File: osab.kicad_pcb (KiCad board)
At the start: 2 copper layers, 60 x 100 mm, 152 parts, among them CON1 TF-01A, CON2 PJ-3420-A-SMT, CON3 TYPE-C-31-M-12, Q1 BC847B, SW1 PPP, SW10 RESET, SW2 VOL-, SW3 VOL+, SW4 CHAP-, SW5 CHAP+, SW6 OT/NT, SW7 BOOK-, SW8 BOOK+, SW9 BUTTON_LOCK, U1 VS1000, U2 ME6211C33M5G-N, U3 25LC640A, U4 TP4055, U5 MF5853CS, U6 TCS7191, Y1 12MHz

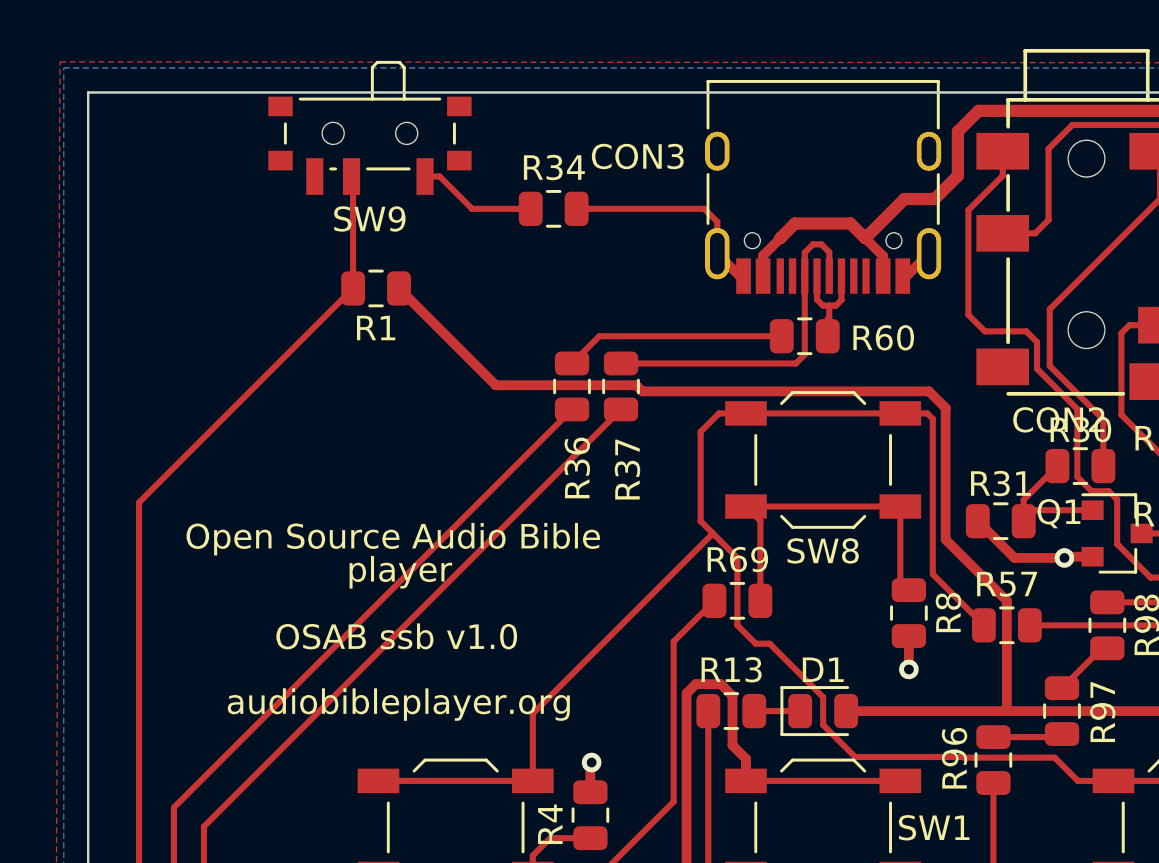
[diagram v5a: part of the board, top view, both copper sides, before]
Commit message: single-sided: Moved button lock back 5.75 mm
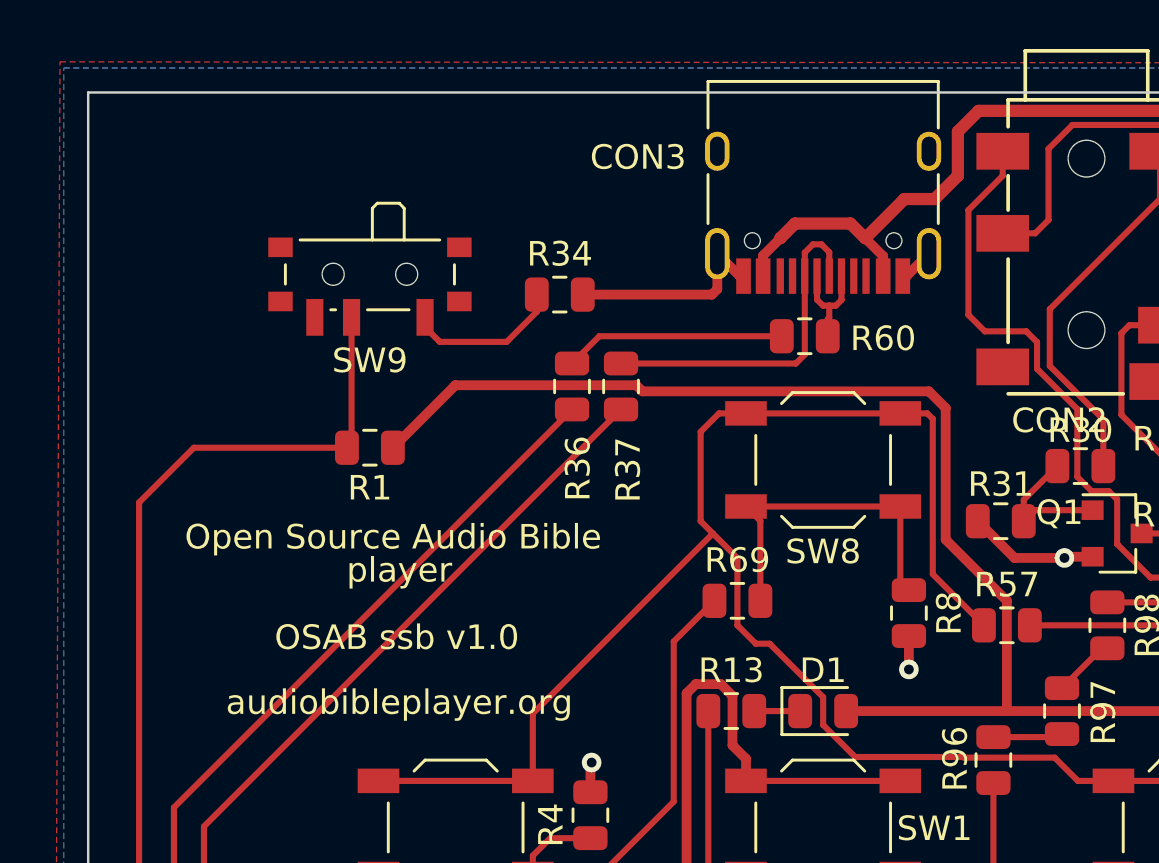
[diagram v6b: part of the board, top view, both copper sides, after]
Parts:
- moved R1 6.50 mm to (126.5, 61.5)
- moved SW9 5.75 mm to (126.5, 54.8)
- moved R34 3.51 mm to (134.2, 55.2)
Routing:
- net Net-(R1-Pad2): track 57.9 -> 55.8 mm
- net Net-(R34-Pad1): track 4.86 -> 6.42 mm
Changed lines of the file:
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@@
     (thickness 1.6)
     (drawings 12)
-    (tracks 1110)
+    (tracks 1111)
     (zones 0)
     (modules 152)
@@
   )
   (module Button_Switch_SMD:SW_SPDT_PCM12 (layer F.Cu)
-    (at 126.5 49 180)
+    (at 126.5 54.75 180)
     (descr "Ultraminiature Surface Mount Slide Switch, right-angle, https://www.ckswitches.com/media/1424/pcm.pdf")
     (attr smd)
@@
   )
   (module Resistor_SMD:R_0805_2012Metric (layer F.Cu)
-    (at 126.75 55 180)
+    (at 126.5 61.5 180)
     (descr "Resistor SMD 0805 (2012 Metric), square (rectangular) end terminal, IPC_7351 nominal, (Body size source: https://docs.google.com/spreadsheets/d/1BsfQQcO9C6DZCsRaXUlFlo91Tg2WpOkGARC1WS5S8t0/edit?usp=sharing), generated with kicad-footprint-generator")
     (tags resistor)
@@
   )
   (module Resistor_SMD:R_0805_2012Metric (layer F.Cu)
-    (at 134 51.75)
+    (at 134.25 55.25)
     (descr "Resistor SMD 0805 (2012 Metric), square (rectangular) end terminal, IPC_7351 nominal, (Body size source: https://docs.google.com/spreadsheets/d/1BsfQQcO9C6DZCsRaXUlFlo91Tg2WpOkGARC1WS5S8t0/edit?usp=sharing), generated with kicad-footprint-generator")
     (tags resistor)
@@
   (segment (start 148.405 54.495) (end 149.32 53.58) (width 0.4) (layer F.Cu) (net 2) (status 30))
   (segment (start 148.25 54.495) (end 148.405 54.495) (width 0.4) (layer F.Cu) (net 2) (status 30))
-  (segment (start 140.68 52.28) (end 140.68 53.58) (width 0.25) (layer F.Cu) (net 2))
-  (segment (start 140.15 51.75) (end 140.68 52.28) (width 0.25) (layer F.Cu) (net 2))
-  (segment (start 134.9375 51.75) (end 140.15 51.75) (width 0.25) (layer F.Cu) (net 2))
+  (segment (start 140.68 55.03) (end 140.68 53.58) (width 0.4) (layer F.Cu) (net 2))
+  (segment (start 140.46 55.25) (end 140.68 55.03) (width 0.4) (layer F.Cu) (net 2))
+  (segment (start 135.1875 55.25) (end 140.46 55.25) (width 0.4) (layer F.Cu) (net 2))
   (segment (start 146.1 127.0875) (end 146.9375 126.25) (width 0.25) (layer F.Cu) (net 3) (status 20))
   (segment (start 146.1 128.15) (end 146.1 127.0875) (width 0.25) (layer F.Cu) (net 3) (status 10))
@@
   (segment (start 140.29999 121.372926) (end 140.29999 119.95001) (width 0.4) (layer F.Cu) (net 8))
   (segment (start 139.822906 121.85001) (end 140.29999 121.372926) (width 0.4) (layer F.Cu) (net 8))
-  (segment (start 150 59.879998) (end 150 65.25) (width 0.4) (layer F.Cu) (net 8))
-  (segment (start 150 65.25) (end 152.5 67.75) (width 0.4) (layer F.Cu) (net 8))
-  (segment (start 149.320001 59.199999) (end 150 59.879998) (width 0.4) (layer F.Cu) (net 8))
-  (segment (start 137.622915 59.199999) (end 149.320001 59.199999) (width 0.4) (layer F.Cu) (net 8))
   (segment (start 145.9375 72.25) (end 152.5 72.25) (width 0.4) (layer F.Cu) (net 8) (status 10))
-  (segment (start 131.63751 58.95001) (end 137.372926 58.95001) (width 0.4) (layer F.Cu) (net 8))
-  (segment (start 152.5 67.75) (end 152.5 72.25) (width 0.4) (layer F.Cu) (net 8))
-  (segment (start 127.6875 55) (end 131.63751 58.95001) (width 0.4) (layer F.Cu) (net 8) (status 10))
-  (segment (start 137.372926 58.95001) (end 137.622915 59.199999) (width 0.4) (layer F.Cu) (net 8))
   (segment (start 162.5 72.25) (end 152.5 72.25) (width 0.4) (layer F.Cu) (net 8))
   (segment (start 169.5 79.25) (end 162.5 72.25) (width 0.4) (layer F.Cu) (net 8))
@@
   (segment (start 150 120.25) (end 150.149999 120.399999) (width 0.5) (layer F.Cu) (net 8))
   (segment (start 147.45 117.75) (end 147.95 117.75) (width 0.25) (layer F.Cu) (net 8))
+  (segment (start 129.98749 58.95001) (end 127.4375 61.5) (width 0.4) (layer F.Cu) (net 8))
+  (segment (start 137.372926 58.95001) (end 129.98749 58.95001) (width 0.4) (layer F.Cu) (net 8))
+  (segment (start 137.622915 59.199999) (end 137.372926 58.95001) (width 0.4) (layer F.Cu) (net 8))
+  (segment (start 152.5 67.75) (end 150 65.25) (width 0.4) (layer F.Cu) (net 8))
+  (segment (start 152.5 72.25) (end 152.5 67.75) (width 0.4) (layer F.Cu) (net 8))
+  (segment (start 150 65.25) (end 150 59.879998) (width 0.4) (layer F.Cu) (net 8))
+  (segment (start 150 59.879998) (end 149.320001 59.199999) (width 0.4) (layer F.Cu) (net 8))
+  (segment (start 149.320001 59.199999) (end 137.622915 59.199999) (width 0.4) (layer F.Cu) (net 8))
   (segment (start 158.1625 116.25) (end 154.6625 116.25) (width 0.25) (layer F.Cu) (net 9) (status 30))
   (segment (start 157.975 130.6875) (end 160.1 130.6875) (width 0.4) (layer F.Cu) (net 10) (status 30))
@@
   (segment (start 165.7125 65.6) (end 166.3125 65) (width 0.25) (layer F.Cu) (net 28) (status 20))
   (segment (start 161.43315 65.6) (end 165.7125 65.6) (width 0.25) (layer F.Cu) (net 28))
-  (segment (start 125.8125 50.4925) (end 125.75 50.43) (width 0.25) (layer F.Cu) (net 29) (status 30))
-  (segment (start 125.8125 55) (end 125.8125 50.4925) (width 0.25) (layer F.Cu) (net 29) (status 30))
-  (segment (start 125.326973 55.485527) (end 125.8125 55) (width 0.25) (layer F.Cu) (net 29) (status 20))
-  (segment (start 117.076973 63.735527) (end 125.326973 55.485527) (width 0.25) (layer F.Cu) (net 29))
   (segment (start 117.076973 104.014473) (end 117.076973 63.735527) (width 0.25) (layer F.Cu) (net 29))
   (segment (start 117.5625 104.5) (end 117.076973 104.014473) (width 0.25) (layer F.Cu) (net 29) (status 10))
+  (segment (start 119.3125 61.5) (end 125.5625 61.5) (width 0.25) (layer F.Cu) (net 29))
+  (segment (start 117.076973 63.735527) (end 119.3125 61.5) (width 0.25) (layer F.Cu) (net 29))
+  (segment (start 125.75 61.3125) (end 125.5625 61.5) (width 0.25) (layer F.Cu) (net 29))
+  (segment (start 125.75 56.18) (end 125.75 61.3125) (width 0.25) (layer F.Cu) (net 29))
   (segment (start 122.95 98.9) (end 128.15 98.9) (width 0.25) (layer F.Cu) (net 30) (status 20))
   (segment (start 121.85 98.9) (end 122.95 98.9) (width 0.25) (layer F.Cu) (net 30) (status 10))
@@
   (segment (start 136.5 140.3125) (end 136.4375 140.25) (width 0.25) (layer F.Cu) (net 45) (status 30))
   (segment (start 136.5 143.5625) (end 136.5 140.3125) (width 0.25) (layer F.Cu) (net 45) (status 30))
-  (segment (start 130.67 51.75) (end 132.575 51.75) (width 0.25) (layer F.Cu) (net 46) (status 20))
-  (segment (start 129.35 50.43) (end 130.67 51.75) (width 0.25) (layer F.Cu) (net 46))
-  (segment (start 132.575 51.75) (end 133.0625 51.75) (width 0.25) (layer F.Cu) (net 46) (status 30))
-  (segment (start 128.75 50.43) (end 129.35 50.43) (width 0.25) (layer F.Cu) (net 46) (status 10))
+  (segment (start 128.75 56.58) (end 128.75 56.18) (width 0.25) (layer F.Cu) (net 46))
+  (segment (start 132.0825 57.18) (end 129.35 57.18) (width 0.25) (layer F.Cu) (net 46))
+  (segment (start 133.3125 55.95) (end 132.0825 57.18) (width 0.25) (layer F.Cu) (net 46))
+  (segment (start 129.35 57.18) (end 128.75 56.58) (width 0.25) (layer F.Cu) (net 46))
+  (segment (start 133.3125 55.25) (end 133.3125 55.95) (width 0.25) (layer F.Cu) (net 46))
   (segment (start 119.199978 101.184932) (end 119.199978 92.815068) (width 0.25) (layer F.Cu) (net 47))
   (segment (start 121.815068 103.800022) (end 119.199978 101.184932) (width 0.25) (layer F.Cu) (net 47))

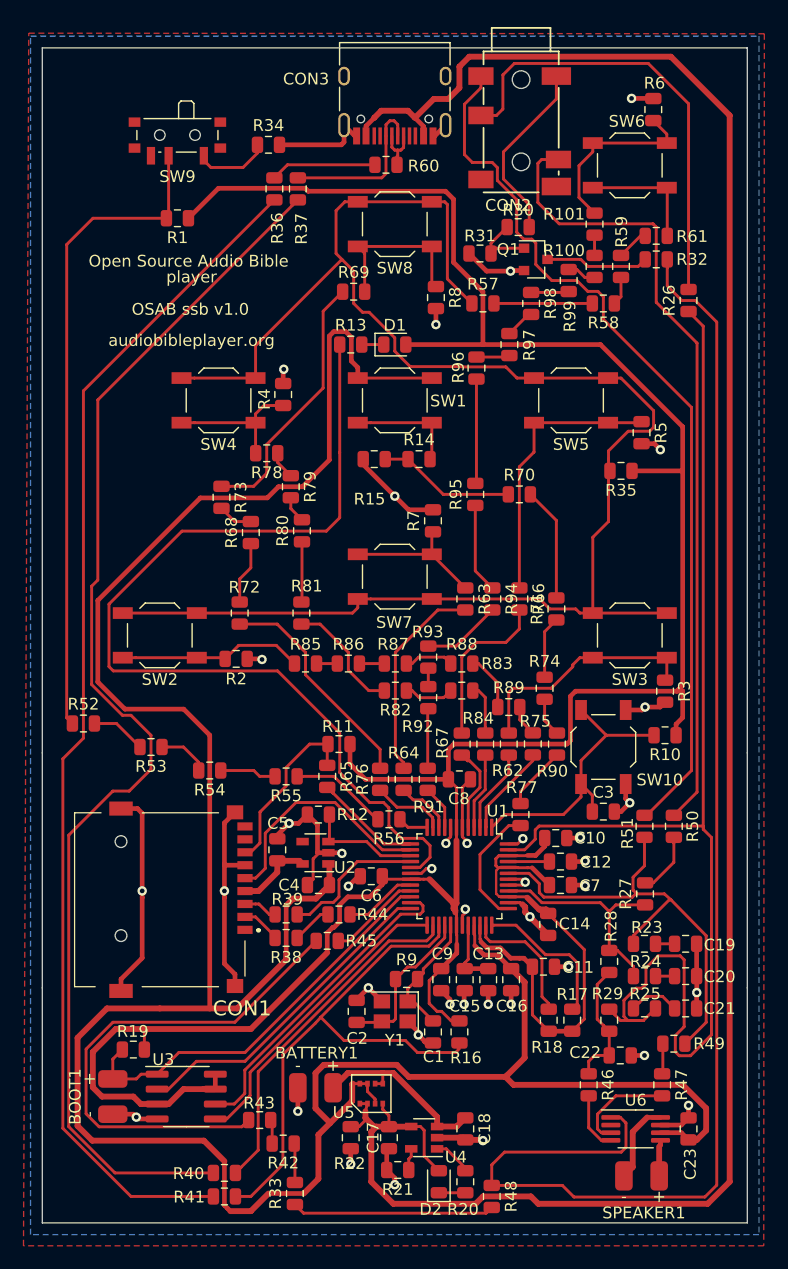
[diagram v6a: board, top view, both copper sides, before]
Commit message: single-sided: Added mounting holes
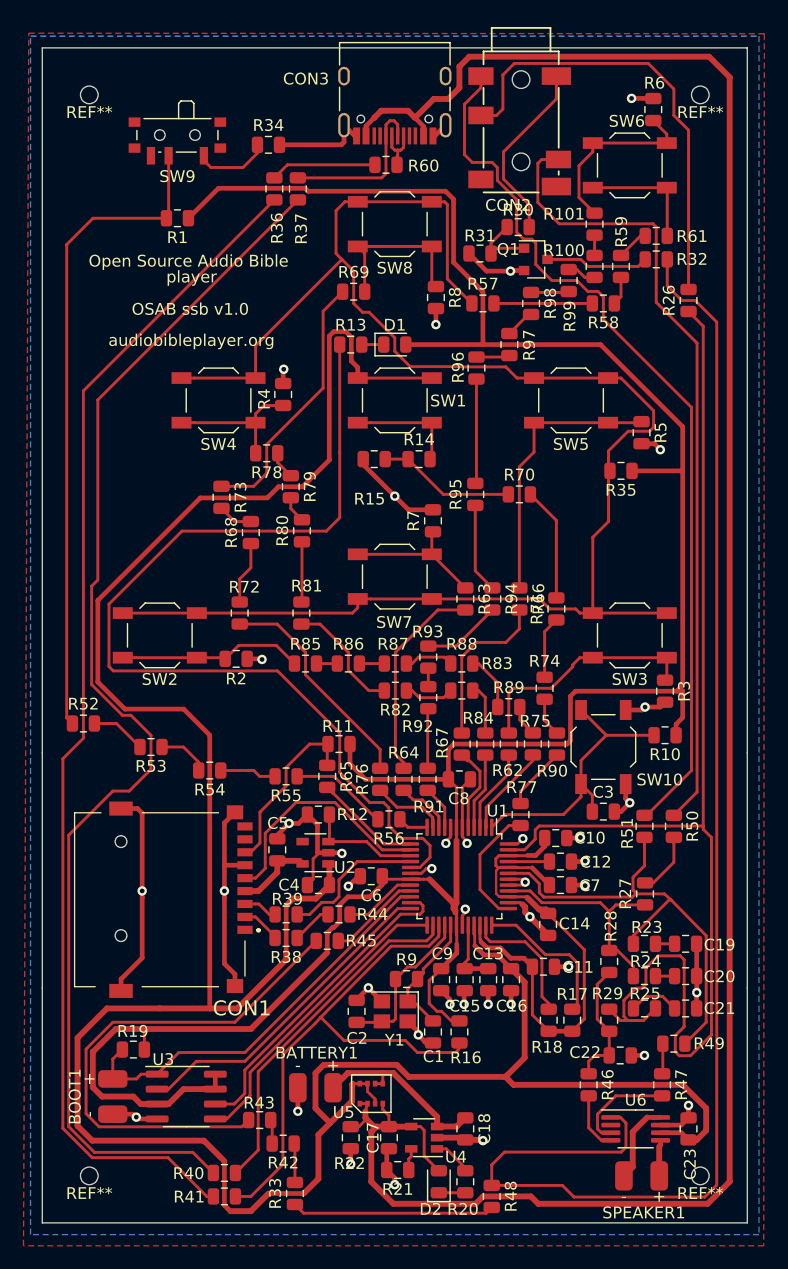
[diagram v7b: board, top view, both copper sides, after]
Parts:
- added REF**: NPTH-1.5, OSAB:NPTH-1.5, F.Cu at (171.0, 143.0)
- added REF**: NPTH-1.5, OSAB:NPTH-1.5, F.Cu at (119.0, 143.0)
- added REF**: NPTH-1.5, OSAB:NPTH-1.5, F.Cu at (119.0, 51.0)
- added REF**: NPTH-1.5, OSAB:NPTH-1.5, F.Cu at (171.0, 51.0)
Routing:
- net Net-(C17-Pad1): track 183.0 -> 185.0 mm

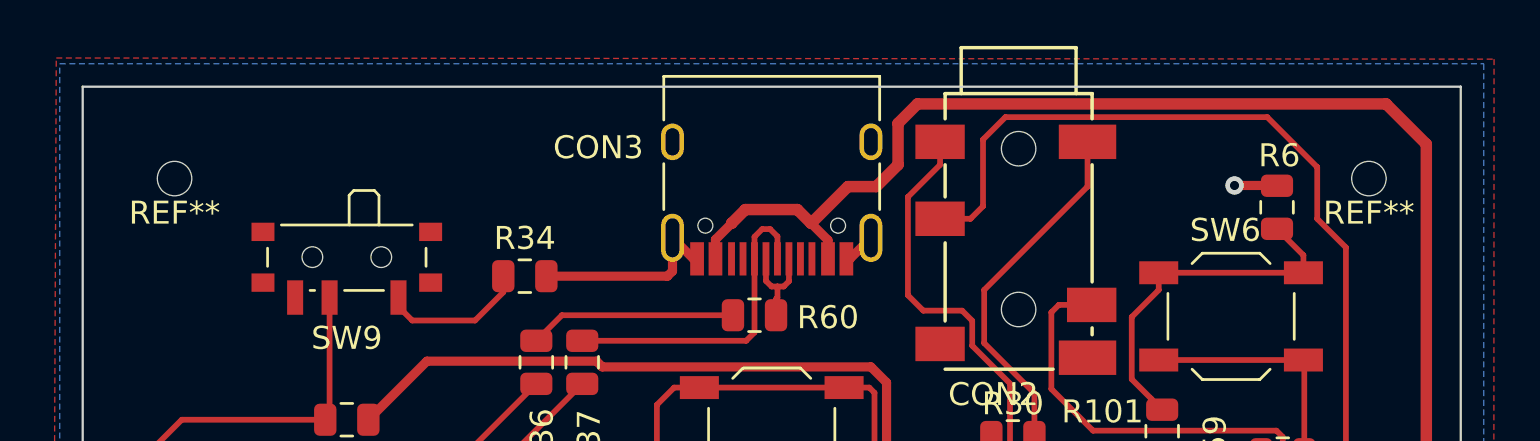
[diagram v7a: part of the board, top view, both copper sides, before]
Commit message: single-sided: Got rid of mounting holes at the top
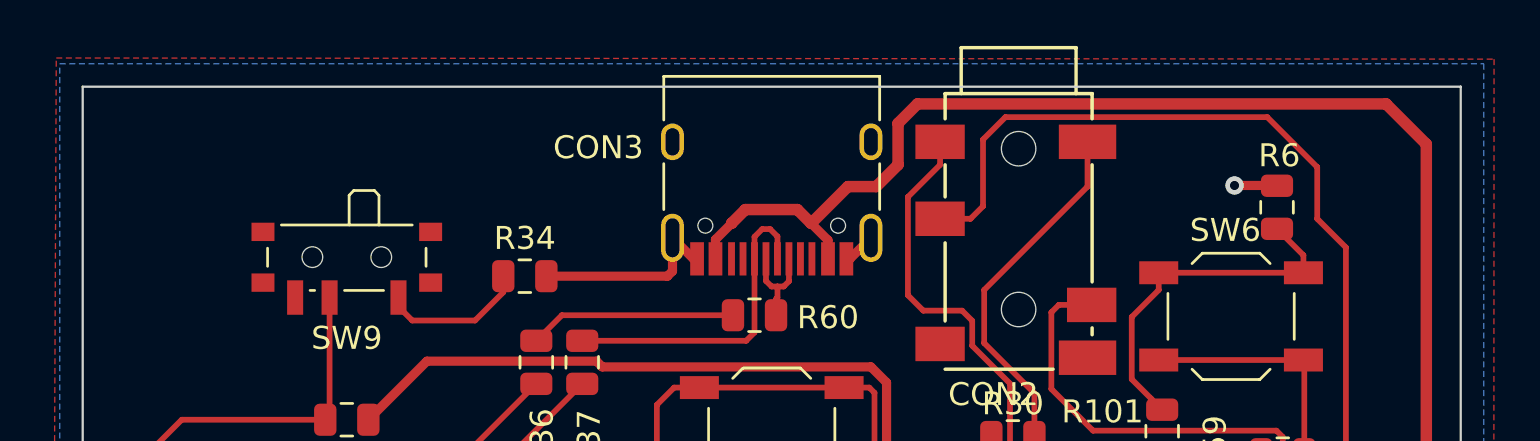
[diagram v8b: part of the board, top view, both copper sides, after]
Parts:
- removed the REF** at (119.0, 51.0)
- removed the REF** at (171.0, 51.0)
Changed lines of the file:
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@@
     (tracks 1115)
     (zones 0)
-    (modules 156)
+    (modules 154)
     (nets 125)
   )
@@
     (fp_text reference REF** (at 0 1.5) (layer F.SilkS)
       (effects (font (size 1 1) (thickness 0.15)))
-    )
-    (fp_text value NPTH-1.5 (at 0 -1.5) (layer F.Fab)
-      (effects (font (size 1 1) (thickness 0.15)))
-    )
-    (pad "" np_thru_hole circle (at 0 0) (size 1.5 1.5) (drill 1.5) (layers *.Cu *.Mask))
-  )
-  (module OSAB:NPTH-1.5 (layer F.Cu)
-    (at 119 51)
-    (fp_text reference REF** (at 0 1.5) (layer F.SilkS)
-      (effects (font (size 1 1) (thickness 0.15)))
-    )
-    (fp_text value NPTH-1.5 (at 0 -1.5) (layer F.Fab)
-      (effects (font (size 1 1) (thickness 0.15)))
-    )
-    (pad "" np_thru_hole circle (at 0 0) (size 1.5 1.5) (drill 1.5) (layers *.Cu *.Mask))
-  )
-  (module OSAB:NPTH-1.5 (layer F.Cu)
-    (at 171 51)
-    (fp_text reference REF** (at 0 1.5) (layer F.SilkS)
-      (effects (font (size 1 1) (thickness 0.15)))
